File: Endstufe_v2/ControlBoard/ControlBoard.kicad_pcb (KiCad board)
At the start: 4 copper layers, 100 x 85 mm, 229 parts, among them J1 B4B-XH-2_(LF)(SN), J10 DNP, J11 DNP, J12 DNP, J13 DNP, J14 DAC all outputs, J15 B4B-XH-2_(LF)(SN), J16 B6B-XH-2(LF)(SN), J2 B4B-XH-2_(LF)(SN), J3 B4B-XH-2_(LF)(SN), J4 DNP, J5 B6B-XH-2(LF)(SN), J6 Conn_01x02_Pin, J7 DNP, J8 DNP, J9 DNP, SW1 TS-1187A-B-A-B, SW2 TS-1187A-B-A-B, U1 NVTFWS014P04M8LTAG, U10 ADAU1962AWBSTZ, U2 1SMA5927A, U3 TPS62933, U4 TYPE-C 16PFS 2JCB1.2-H6.5 IPX8, U5 W25Q128JVS, U6 RP2040, U7 W25Q128JVS, U8 ADAU1467WBCPZ300, U9 ZPLR135_T8, Y1 12Mhz, Y2 24.576Mhz, Y3 24.576Mhz

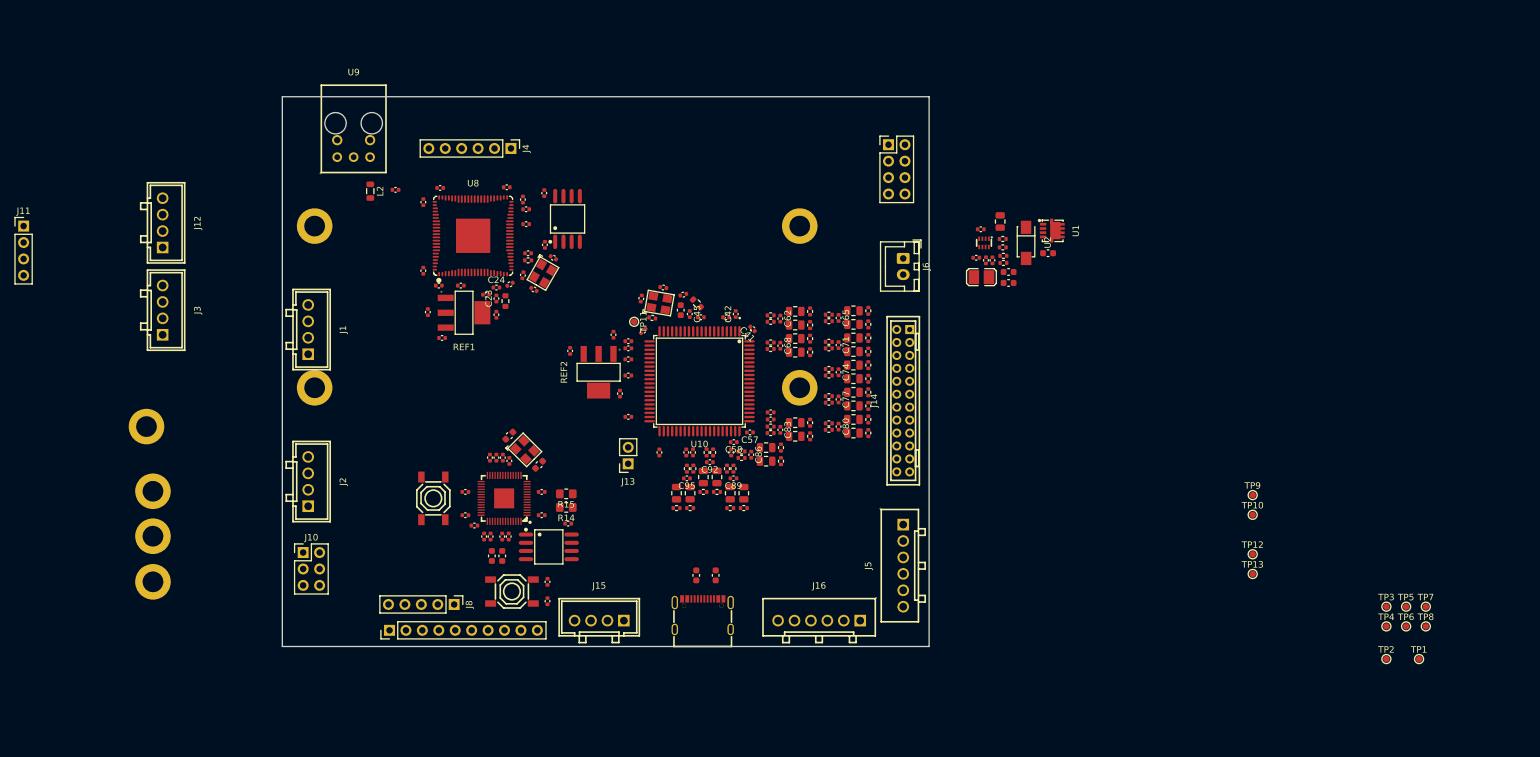
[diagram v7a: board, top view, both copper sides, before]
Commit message: Enlargen Amplifier Board to make space for mounting holes
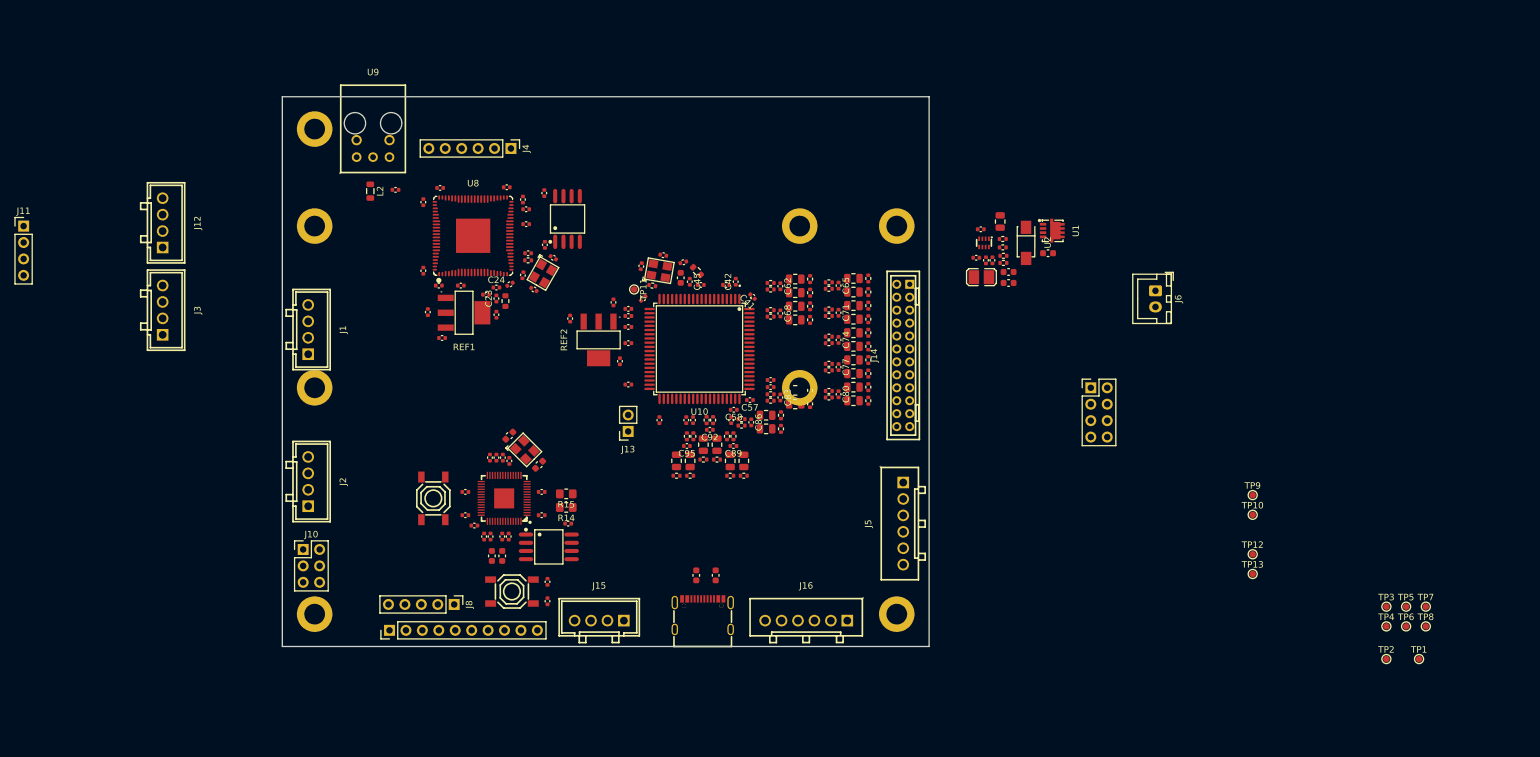
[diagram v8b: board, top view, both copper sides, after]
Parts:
- moved H5 122.1 mm to (165.0, 90.0)
- moved H8 115.1 mm to (165.0, 150.0)
- moved H6 52.8 mm to (75.0, 75.0)
- moved J7 48.9 mm to (195.0, 115.0)
- moved J6 39.3 mm to (205.0, 100.0)
- moved H7 27.8 mm to (75.0, 150.0)
- moved J14 7.00 mm to (166.0, 110.0)
- moved J5 6.50 mm to (166.0, 136.0)
- moved C90 5.00 mm to (139.2, 126.3)
- moved C91 5.00 mm to (141.3, 126.3)
- moved C93 5.00 mm to (135.1, 123.8)
- moved C94 5.00 mm to (137.2, 123.8)
- moved C96 5.00 mm to (131.0, 126.3)
- moved C97 5.00 mm to (133.1, 126.3)
- moved C100 5.00 mm to (114.5, 104.3)
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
